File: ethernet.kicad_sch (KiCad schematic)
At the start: 49 parts, among them J401 JK0654219, U401 MIC23050-4YML, U402 KSZ9031RNXCA, U403 ASDMB-25.000MHz, U404 74LVC2G07

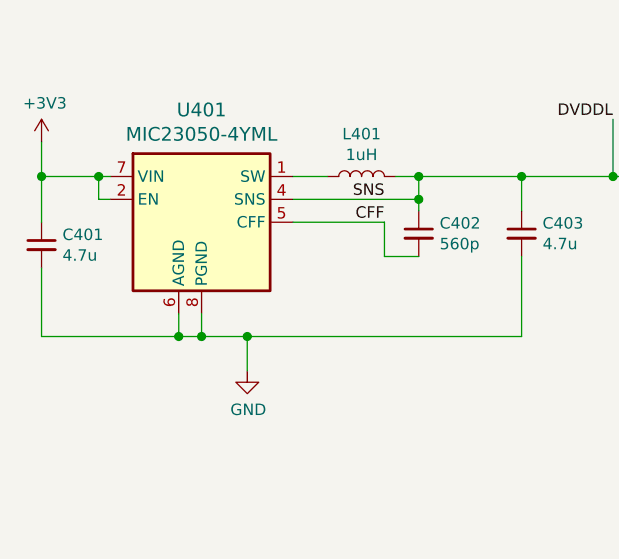
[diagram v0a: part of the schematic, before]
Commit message: Layout Ethernet core power regulator
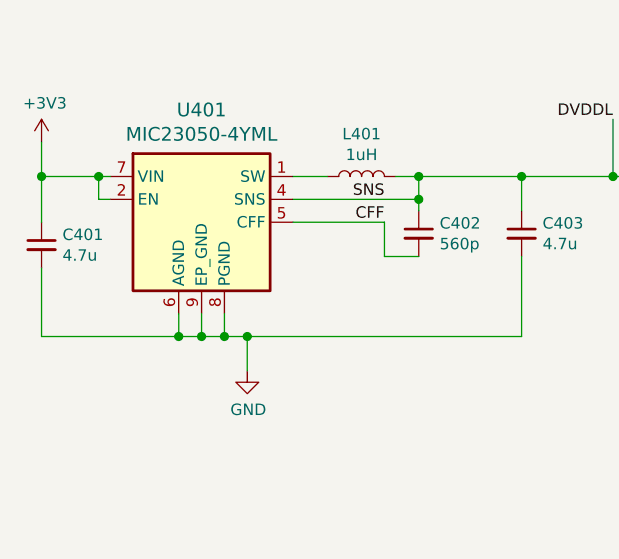
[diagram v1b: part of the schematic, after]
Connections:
- net GND: now also U401.9 (EP_GND)
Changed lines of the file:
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@@
   (junction (at 48.26 54.61) (diameter 1.016) (color 0 0 0 0))
   (junction (at 50.8 54.61) (diameter 1.016) (color 0 0 0 0))
+  (junction (at 53.34 54.61) (diameter 1.016) (color 0 0 0 0))
   (junction (at 55.88 54.61) (diameter 1.016) (color 0 0 0 0))
   (junction (at 74.93 36.83) (diameter 1.016) (color 0 0 0 0))
@@
     (stroke (width 0) (type solid) (color 0 0 0 0))
   )
-  (wire (pts (xy 50.8 54.61) (xy 55.88 54.61))
+  (wire (pts (xy 50.8 54.61) (xy 53.34 54.61))
     (stroke (width 0) (type solid) (color 0 0 0 0))
   )
+  (wire (pts (xy 53.34 52.07) (xy 53.34 54.61))
+    (stroke (width 0) (type solid) (color 0 0 0 0))
+  )
+  (wire (pts (xy 53.34 54.61) (xy 55.88 54.61))
+    (stroke (width 0) (type solid) (color 0 0 0 0))
+  )

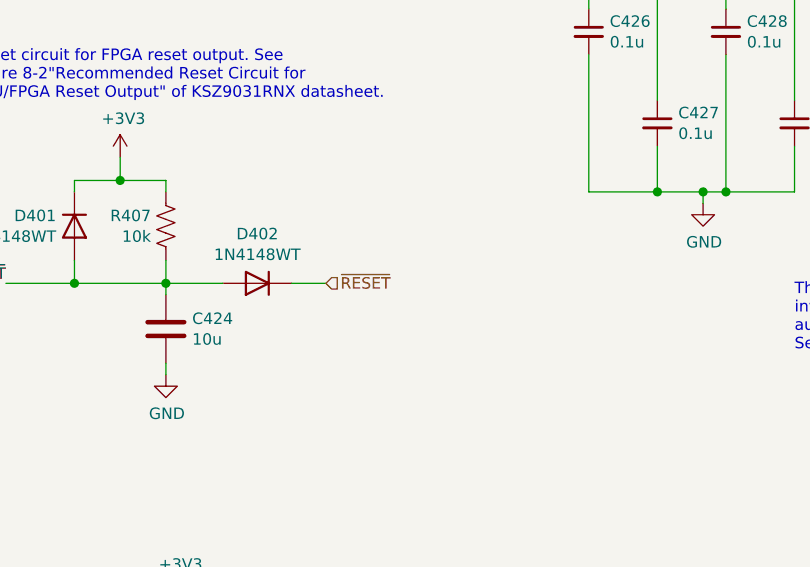
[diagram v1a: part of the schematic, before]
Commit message: Layout Ethernet clock and pull-up resistors
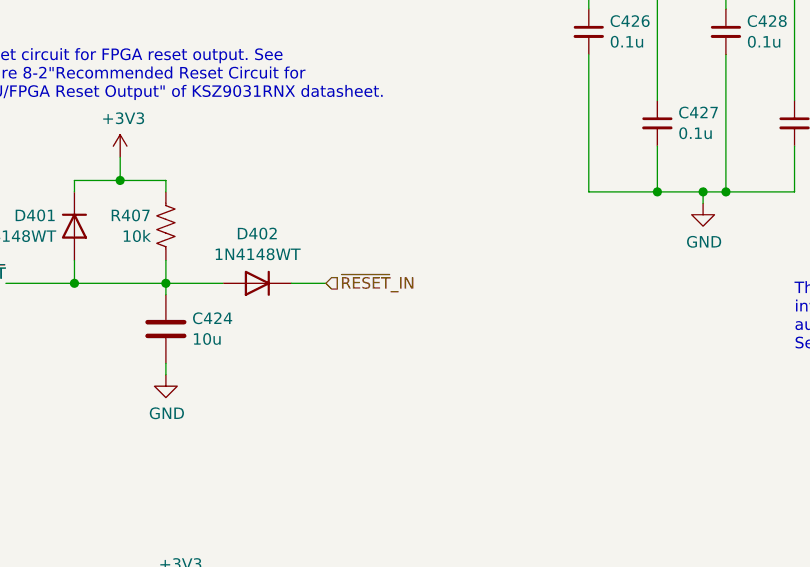
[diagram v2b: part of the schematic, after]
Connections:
- net ~RESET renamed ~RESET~_IN
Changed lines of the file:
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@@
     (effects (font (size 1.27 1.27)) (justify right))
   )
-  (hierarchical_label "~RESET" (shape input) (at 285.75 157.48 0)
+  (hierarchical_label "~RESET~_IN" (shape input) (at 285.75 157.48 0)
     (effects (font (size 1.27 1.27)) (justify left))
   )

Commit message: Route ULPI signals
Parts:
- R408, R409: footprint Resistor_SMD:R_0603_1608Metric -> Resistor_SMD:R_0402_1005Metric
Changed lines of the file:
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@@
       (effects (font (size 1.27 1.27)) (justify right))
     )
-    (property "Footprint" "Resistor_SMD:R_0603_1608Metric" (id 2) (at 346.964 81.026 90)
+    (property "Footprint" "Resistor_SMD:R_0402_1005Metric" (id 2) (at 346.964 81.026 90)
       (effects (font (size 1.27 1.27)) hide)
     )
@@
     (property "Reference" "R409" (id 0) (at 349.25 137.4204 90))
     (property "Value" "75" (id 1) (at 349.25 139.7191 90))
-    (property "Footprint" "Resistor_SMD:R_0603_1608Metric" (id 2) (at 348.996 135.636 90)
+    (property "Footprint" "Resistor_SMD:R_0402_1005Metric" (id 2) (at 348.996 135.636 90)
       (effects (font (size 1.27 1.27)) hide)
     )
